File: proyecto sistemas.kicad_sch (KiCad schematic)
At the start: 0 parts

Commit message: unifilar nuevo 10/13/2025
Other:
- note added: "10 mm2"
- note added: "11 m"
- note added: "13,25 A"
- note added: "14,55 A"
- note added: "16 mm2"
- note added: "19,9 m"
- note added: "2,5 mm2"
- note added: "25,8 m"
- note added: "27,5 m"
- note added: "27,8 m"
- note added: "37,2 m"
- note added: "5,7 m"
- note added: "6 mm2"
- note added: "60 m"
- note added: "68,47 A"
- note added: "7,38 A"
- note added: "C7"
- note removed: "11,04 A"
- note removed: "16 m"
- note removed: "197,72 A"
- note removed: "1F + N (T)"
- note removed: "20m"
- note removed: "25,37 A"
- note removed: "28m"
- note removed: "36 m"
- note removed: "4,5 m"
- note removed: "6,5 A"
- note removed: "8 m"

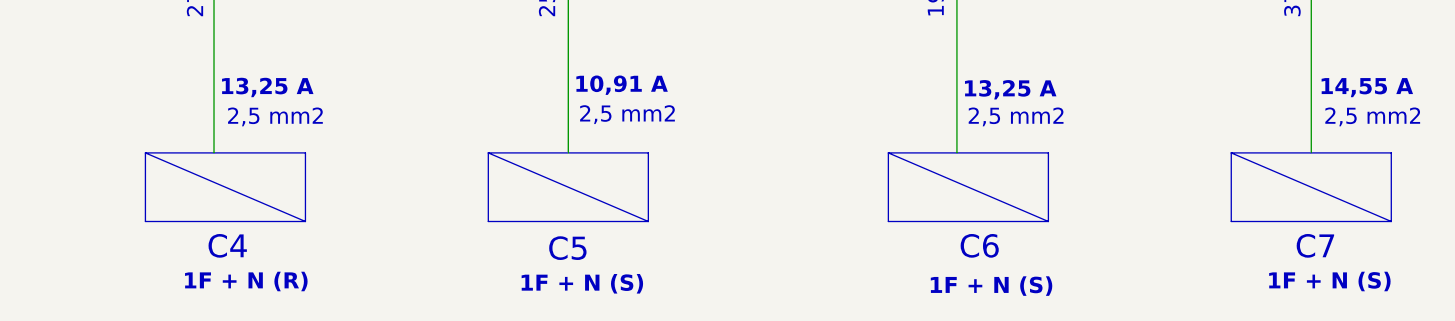
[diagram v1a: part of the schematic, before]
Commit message: fixed names of phases RST
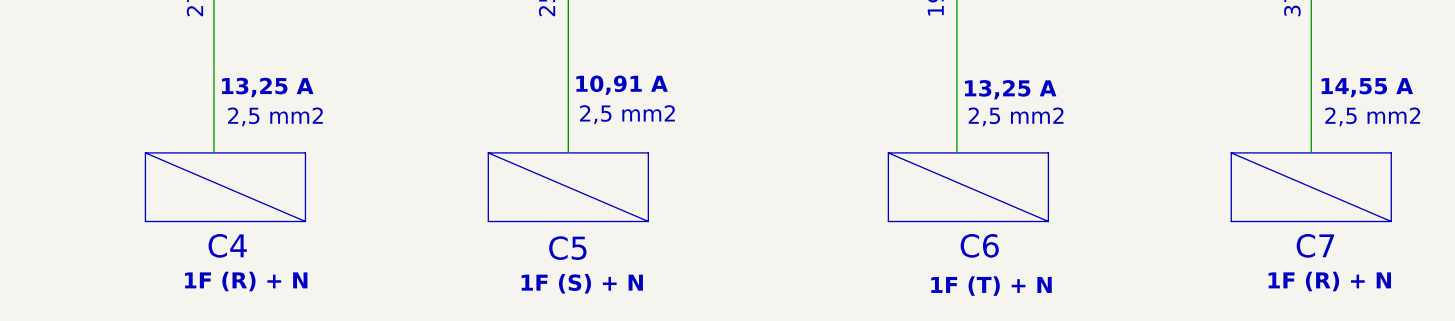
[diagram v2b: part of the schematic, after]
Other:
- note added: "1F (R) + N"
- note added: "1F (S) + N"
- note added: "1F (T) + N"
- note removed: "1F + N (R)"
- note removed: "1F + N (S)"
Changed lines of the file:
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@@
 		)
 	)
-	(text "1F + N (S)"
+	(text "1F (S) + N "
 		(exclude_from_sim no)
 		(at 176.784 143.002 0)
@@
 		)
 	)
-	(text "1F + N (S)"
+	(text "1F (R) + N "
 		(exclude_from_sim no)
 		(at 259.842 142.748 0)
@@
 		)
 	)
-	(text "1F + N (S)"
+	(text "1F (T) + N"
 		(exclude_from_sim no)
 		(at 222.25 143.256 0)
@@
 		)
 	)
-	(text "1F + N (R)"
+	(text "1F (R) + N "
 		(exclude_from_sim no)
 		(at 139.446 142.748 0)
@@
 			)
 		)
-		(column_widths 30.48)
-		(row_heights 3.81 3.81)
+		(column_widths 22.86)
+		(row_heights 3.81 6.35)
 		(cells
-			(table_cell "Horno Selecta HT"
-				(exclude_from_sim no)
-				(at 83.82 146.05 0)
-				(size 30.48 3.81)
-				(margins 0.9525 0.9525 0.9525 0.9525)
-				(span 1 1)
-				(fill
-					(type none)
-				)
-				(effects
-					(font
-						(size 1.778 1.778)
-					)
-					(justify left top)
-				)
-			)
-			(table_cell "1 enchufe pulidora"
-				(exclude_from_sim no)
-				(at 83.82 149.86 0)
-				(size 30.48 3.81)
+			(table_cell "Cronografo Hp"
+				(exclude_from_sim no)
+				(at 209.55 146.05 0)
+				(size 22.86 3.81)
+				(margins 0.9525 0.9525 0.9525 0.9525)
+				(span 1 1)
+				(fill
+					(type none)
+				)
+				(effects
+					(font
+						(size 1.778 1.778)
+					)
+					(justify left top)
+				)
+			)
+			(table_cell "Cromotografo Metrohm"
+				(exclude_from_sim no)
+				(at 209.55 149.86 0)
+				(size 22.86 6.35)
 				(margins 0.9525 0.9525 0.9525 0.9525)
 				(span 1 1)
@@
 			)
 		)
-		(column_widths 22.86)
-		(row_heights 6.35 5.08 6.35)
+		(column_widths 33.02)
+		(row_heights 5.08 5.08)
 		(cells
-			(table_cell "Centrifugadora Merck"
-				(exclude_from_sim no)
-				(at 248.92 146.05 0)
-				(size 22.86 6.35)
-				(margins 0.9525 0.9525 0.9525 0.9525)
-				(span 1 1)
-				(fill
-					(type none)
-				)
-				(effects
-					(font
-						(size 1.778 1.778)
-					)
-					(justify left top)
-				)
-			)
-			(table_cell "Agitadora Velp"
-				(exclude_from_sim no)
-				(at 248.92 152.4 0)
-				(size 22.86 5.08)
-				(margins 0.9525 0.9525 0.9525 0.9525)
-				(span 1 1)
-				(fill
-					(type none)
-				)
-				(effects
-					(font
-						(size 1.778 1.778)
-					)
-					(justify left top)
-				)
-			)
-			(table_cell "Cromotografo Metrohm"
-				(exclude_from_sim no)
-				(at 248.92 157.48 0)
-				(size 22.86 6.35)
+			(table_cell "Agitadoras Velp"
+				(exclude_from_sim no)
+				(at 120.65 146.05 0)
+				(size 33.02 5.08)
+				(margins 0.9525 0.9525 0.9525 0.9525)
+				(span 1 1)
+				(fill
+					(type none)
+				)
+				(effects
+					(font
+						(size 1.778 1.778)
+					)
+					(justify left top)
+				)
+			)
+			(table_cell "Centrifugadoras Merck"
+				(exclude_from_sim no)
+				(at 120.65 151.13 0)
+				(size 33.02 5.08)
 				(margins 0.9525 0.9525 0.9525 0.9525)
 				(span 1 1)
@@
 			)
 		)
-		(column_widths 22.86)
-		(row_heights 3.81 6.35)
+		(column_widths 24.13)
+		(row_heights 6.35 6.35)
 		(cells
-			(table_cell "Cronografo Hp"
-				(exclude_from_sim no)
-				(at 209.55 146.05 0)
-				(size 22.86 3.81)
-				(margins 0.9525 0.9525 0.9525 0.9525)
-				(span 1 1)
-				(fill
-					(type none)
-				)
-				(effects
-					(font
-						(size 1.778 1.778)
-					)
-					(justify left top)
-				)
-			)
-			(table_cell "Cromotografo Metrohm"
-				(exclude_from_sim no)
-				(at 209.55 149.86 0)
-				(size 22.86 6.35)
+			(table_cell "Centrifugadora Selecta"
+				(exclude_from_sim no)
+				(at 52.07 146.05 0)
+				(size 24.13 6.35)
+				(margins 0.9525 0.9525 0.9525 0.9525)
+				(span 1 1)
+				(fill
+					(type none)
+				)
+				(effects
+					(font
+						(size 1.778 1.778)
+					)
+					(justify left top)
+				)
+			)
+			(table_cell "2 enchufes de piladora"
+				(exclude_from_sim no)
+				(at 52.07 152.4 0)
+				(size 24.13 6.35)
 				(margins 0.9525 0.9525 0.9525 0.9525)
 				(span 1 1)
@@
 			)
 		)
-		(column_widths 33.02)
-		(row_heights 5.08 5.08)
+		(column_widths 26.67)
+		(row_heights 3.81 3.81 3.81 3.81 6.35)
 		(cells
-			(table_cell "Agitadoras Velp"
-				(exclude_from_sim no)
-				(at 120.65 146.05 0)
-				(size 33.02 5.08)
-				(margins 0.9525 0.9525 0.9525 0.9525)
-				(span 1 1)
-				(fill
-					(type none)
-				)
-				(effects
-					(font
-						(size 1.778 1.778)
-					)
-					(justify left top)
-				)
-			)
-			(table_cell "Centrifugadoras Merck"
-				(exclude_from_sim no)
-				(at 120.65 151.13 0)
-				(size 33.02 5.08)
+			(table_cell "Horno Selecta"
+				(exclude_from_sim no)
+				(at 163.83 144.78 0)
+				(size 26.67 3.81)
+				(margins 0.9525 0.9525 0.9525 0.9525)
+				(span 1 1)
+				(fill
+					(type none)
+				)
+				(effects
+					(font
+						(size 1.778 1.778)
+					)
+					(justify left top)
+				)
+			)
+			(table_cell "Agitador Selecta"
+				(exclude_from_sim no)
+				(at 163.83 148.59 0)
+				(size 26.67 3.81)
+				(margins 0.9525 0.9525 0.9525 0.9525)
+				(span 1 1)
+				(fill
+					(type none)
+				)
+				(effects
+					(font
+						(size 1.778 1.778)
+					)
+					(justify left top)
+				)
+			)
+			(table_cell "Pantalla"
+				(exclude_from_sim no)
+				(at 163.83 152.4 0)
+				(size 26.67 3.81)
+				(margins 0.9525 0.9525 0.9525 0.9525)
+				(span 1 1)
+				(fill
+					(type none)
+				)
+				(effects
+					(font
+						(size 1.778 1.778)
+					)
+					(justify left top)
+				)
+			)
+			(table_cell "PC"
+				(exclude_from_sim no)
+				(at 163.83 156.21 0)
+				(size 26.67 3.81)
+				(margins 0.9525 0.9525 0.9525 0.9525)
+				(span 1 1)
+				(fill
+					(type none)
+				)
+				(effects
+					(font
+						(size 1.778 1.778)
+					)
+					(justify left top)
+				)
+			)
+			(table_cell "Cromatografo Metrohm"
+				(exclude_from_sim no)
+				(at 163.83 160.02 0)
+				(size 26.67 6.35)
 				(margins 0.9525 0.9525 0.9525 0.9525)
 				(span 1 1)
@@
 			)
 		)
-		(column_widths 26.67)
-		(row_heights 3.81 3.81 3.81 3.81 6.35)
+		(column_widths 30.48)
+		(row_heights 3.81 3.81)
 		(cells
-			(table_cell "Horno Selecta"
-				(exclude_from_sim no)
-				(at 163.83 144.78 0)
-				(size 26.67 3.81)
-				(margins 0.9525 0.9525 0.9525 0.9525)
-				(span 1 1)
-				(fill
-					(type none)
-				)
-				(effects
-					(font
-						(size 1.778 1.778)
-					)
-					(justify left top)
-				)
-			)
-			(table_cell "Agitador Selecta"
-				(exclude_from_sim no)
-				(at 163.83 148.59 0)
-				(size 26.67 3.81)
-				(margins 0.9525 0.9525 0.9525 0.9525)
-				(span 1 1)
-				(fill
-					(type none)
-				)
-				(effects
-					(font
-						(size 1.778 1.778)
-					)
-					(justify left top)
-				)
-			)
-			(table_cell "Pantalla"
-				(exclude_from_sim no)
-				(at 163.83 152.4 0)
-				(size 26.67 3.81)
-				(margins 0.9525 0.9525 0.9525 0.9525)
-				(span 1 1)
-				(fill
-					(type none)
-				)
-				(effects
-					(font
-						(size 1.778 1.778)
-					)
-					(justify left top)
-				)
-			)
-			(table_cell "PC"
-				(exclude_from_sim no)
-				(at 163.83 156.21 0)
-				(size 26.67 3.81)
-				(margins 0.9525 0.9525 0.9525 0.9525)
-				(span 1 1)
-				(fill
-					(type none)
-				)
-				(effects
-					(font
-						(size 1.778 1.778)
-					)
-					(justify left top)
-				)
-			)
-			(table_cell "Cromatografo Metrohm"
-				(exclude_from_sim no)
-				(at 163.83 160.02 0)
-				(size 26.67 6.35)
+			(table_cell "Horno Selecta HT"
+				(exclude_from_sim no)
+				(at 83.82 146.05 0)
+				(size 30.48 3.81)
+				(margins 0.9525 0.9525 0.9525 0.9525)
+				(span 1 1)
+				(fill
+					(type none)
+				)
+				(effects
+					(font
+						(size 1.778 1.778)
+					)
+					(justify left top)
+				)
+			)
+			(table_cell "1 enchufe pulidora"
+				(exclude_from_sim no)
+				(at 83.82 149.86 0)
+				(size 30.48 3.81)
 				(margins 0.9525 0.9525 0.9525 0.9525)
 				(span 1 1)
@@
 			)
 		)
-		(column_widths 24.13)
-		(row_heights 6.35 6.35)
+		(column_widths 22.86)
+		(row_heights 6.35 5.08 6.35)
 		(cells
-			(table_cell "Centrifugadora Selecta"
-				(exclude_from_sim no)
-				(at 52.07 146.05 0)
-				(size 24.13 6.35)
-				(margins 0.9525 0.9525 0.9525 0.9525)
-				(span 1 1)
-				(fill
-					(type none)
-				)
-				(effects
-					(font
-						(size 1.778 1.778)
-					)
-					(justify left top)
-				)
-			)
-			(table_cell "2 enchufes de piladora"
-				(exclude_from_sim no)
-				(at 52.07 152.4 0)
-				(size 24.13 6.35)
-				(margins 0.9525 0.9525 0.9525 0.9525)
-				(span 1 1)
+			(table_cell "Centrifugadora Merck"
+				(exclude_from_sim no)
+				(at 248.92 146.05 0)
+				(size 22.86 6.35)
+				(margins 0.9525 0.9525 0.9525 0.9525)
+				(span 1 1)
+				(fill
+					(type none)
+				)
+				(effects
+					(font
+						(size 1.778 1.778)
+					)
+					(justify left top)
+				)
+			)
+			(table_cell "Agitadora Velp"
+				(exclude_from_sim no)
+				(at 248.92 152.4 0)
+				(size 22.86 5.08)
+				(margins 0.9525 0.9525 0.9525 0.9525)
+				(span 1 1)
+				(fill
+					(type none)
+				)
+				(effects
+					(font
+						(size 1.778 1.778)
+					)
+					(justify left top)
+				)
+			)
+			(table_cell "Cromotografo Metrohm"
+				(exclude_from_sim no)
+				(at 248.92 157.48 0)
+				(size 22.86 6.35)
+				(margins 0.9525 0.9525 0.9525 0.9525)
+				(span 1 1)
